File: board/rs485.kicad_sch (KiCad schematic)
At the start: 6 parts, among them J5 RS486, U5 ST3485EB

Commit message: WIP
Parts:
- J5: footprint Connector_Phoenix_MC:PhoenixContact_MCV_1,5_3-G-3.5_1x03_P3.50mm_Vertical -> Connector_Phoenix_MC:PhoenixContact_MC_1,5_3-G-3.5_1x03_P3.50mm_Horizontal
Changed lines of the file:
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@@
 			)
 		)
-		(property "Footprint" "Connector_Phoenix_MC:PhoenixContact_MCV_1,5_3-G-3.5_1x03_P3.50mm_Vertical"
+		(property "Footprint" "Connector_Phoenix_MC:PhoenixContact_MC_1,5_3-G-3.5_1x03_P3.50mm_Horizontal"
 			(at 173.99 81.28 0)
 			(hide yes)

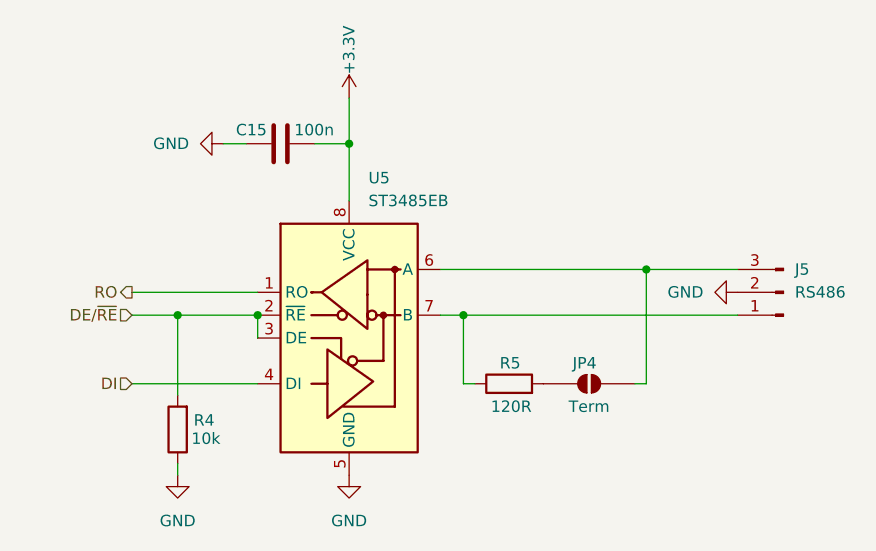
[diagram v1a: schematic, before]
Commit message: Update board settings, schematic components, and add footprint library
- Changed active layer from 0 to 25 and updated hidden nets to include "GND" in at32f455-bob.kicad_prl.
- Modified selection filter settings to hide dimensions, graphics, keepouts, and other items in at32f455-bob.kicad_prl.
- Adjusted visible layers in at32f455-bob.kicad_prl for better clarity.
- Updated the position and orientation of the J5 connector in rs485.kicad_sch for improved layout.
- Added a new fp-lib-table file to define the footprint library for the project.
- Updated submodule reference for hw-kicad to the latest commit.
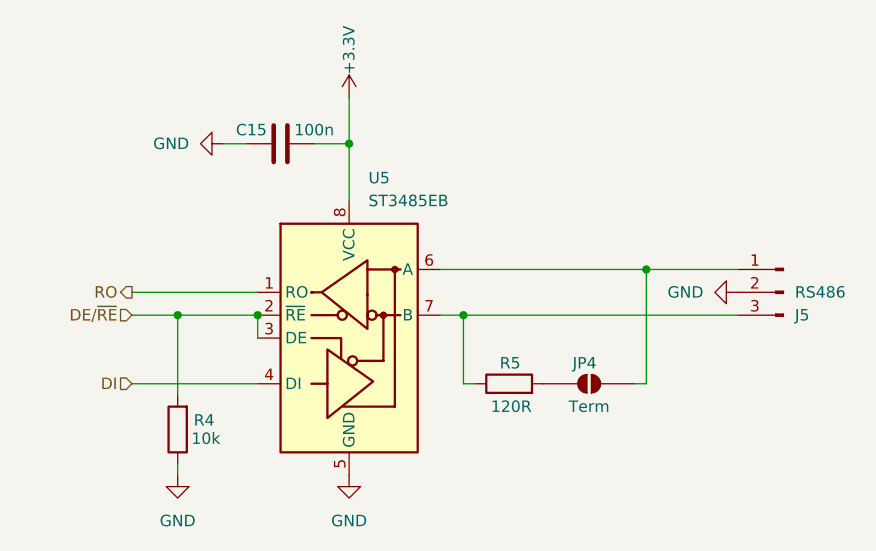
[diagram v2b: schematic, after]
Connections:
- net at JP4.2 (B), U5.6 (A): now also J5.1 (Pin_1); no longer J5.3 (Pin_3)
- net at R5.1, U5.7 (B): now also J5.3 (Pin_3); no longer J5.1 (Pin_1)
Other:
- moved on the sheet: J5
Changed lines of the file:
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@@
 	(symbol
 		(lib_id "Connector:Conn_01x03_Pin")
-		(at 173.99 81.28 180)
+		(at 173.99 81.28 0)
+		(mirror y)
 		(unit 1)
 		(body_style 1)
@@
 		(dnp no)
 		(property "Reference" "J5"
-			(at 175.26 78.7399 0)
+			(at 175.26 83.8201 0)
 			(show_name no)
 			(do_not_autoplace no)
@@
 		)
 		(property "Value" "RS486"
-			(at 175.26 81.2799 0)
+			(at 175.26 81.2801 0)
 			(show_name no)
 			(do_not_autoplace no)
